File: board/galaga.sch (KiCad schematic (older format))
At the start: 20 parts, among them J1 led_a, J2 speaker_out, J3 led_b, J4 led_c, J5 pwr_in, J6 Conn_02x03_Odd_Even, Q1 IRF540N, SW1 SW_Push, U1 LD1117S33TR_SOT223, U2 ATmega328P-PU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

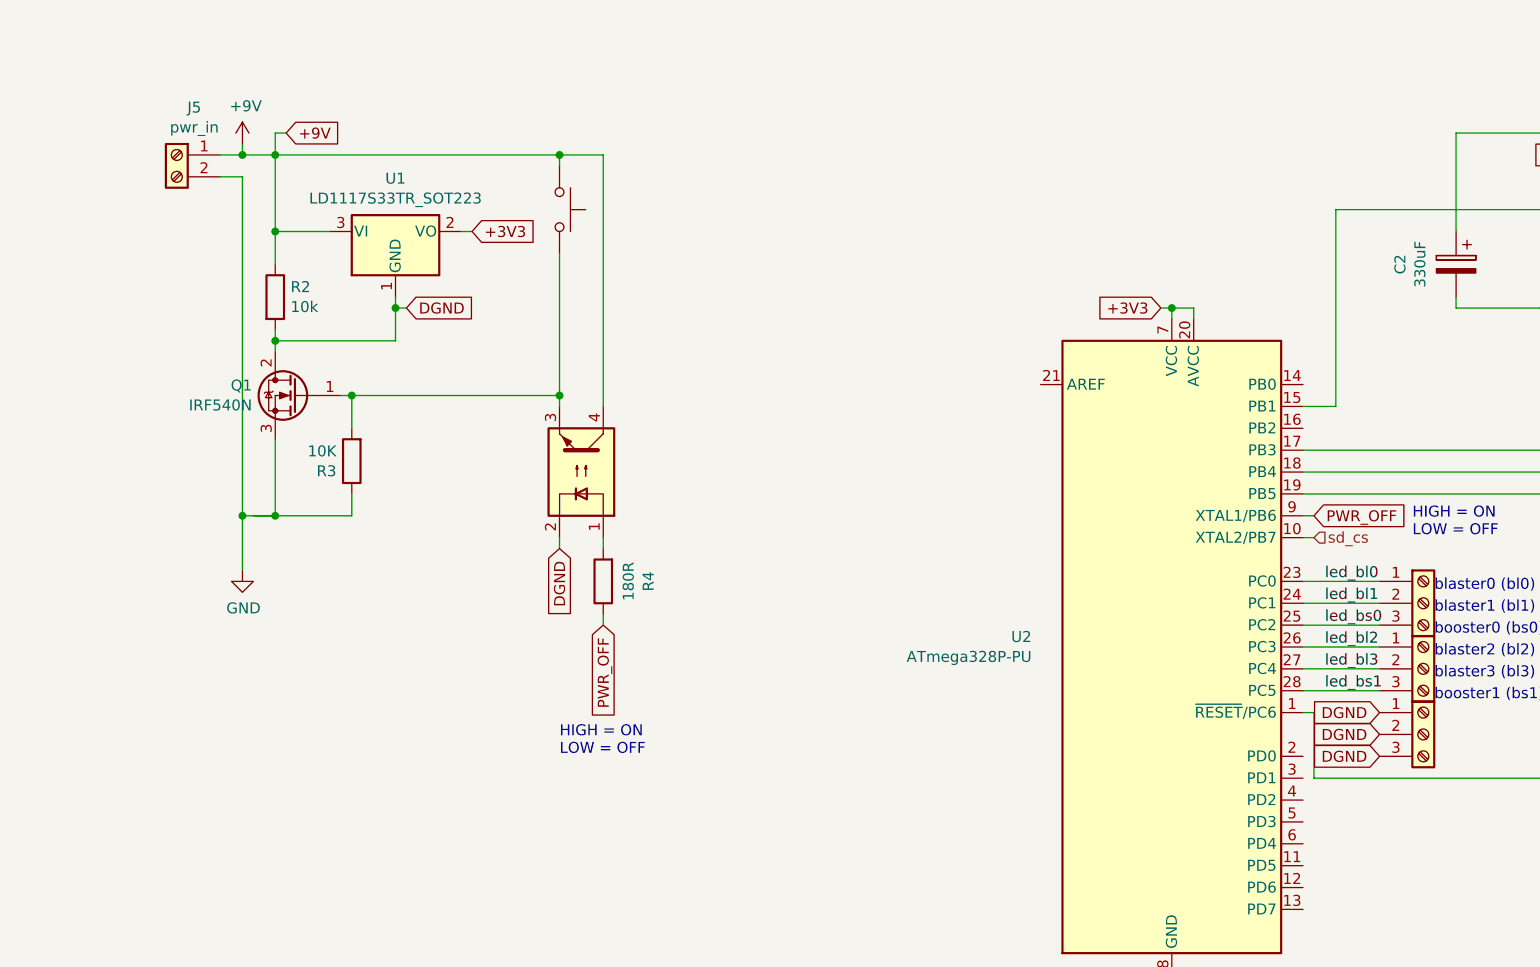
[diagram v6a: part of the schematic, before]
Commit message: RNG tweaked, tested, and working!
All that's really left now is to make the lights flash and assemble
everything. Making the while loop break at the end of file flag instad
of polling seems to have fixed the no-power-off issue - it powered off
perfectly 100 times in a row!
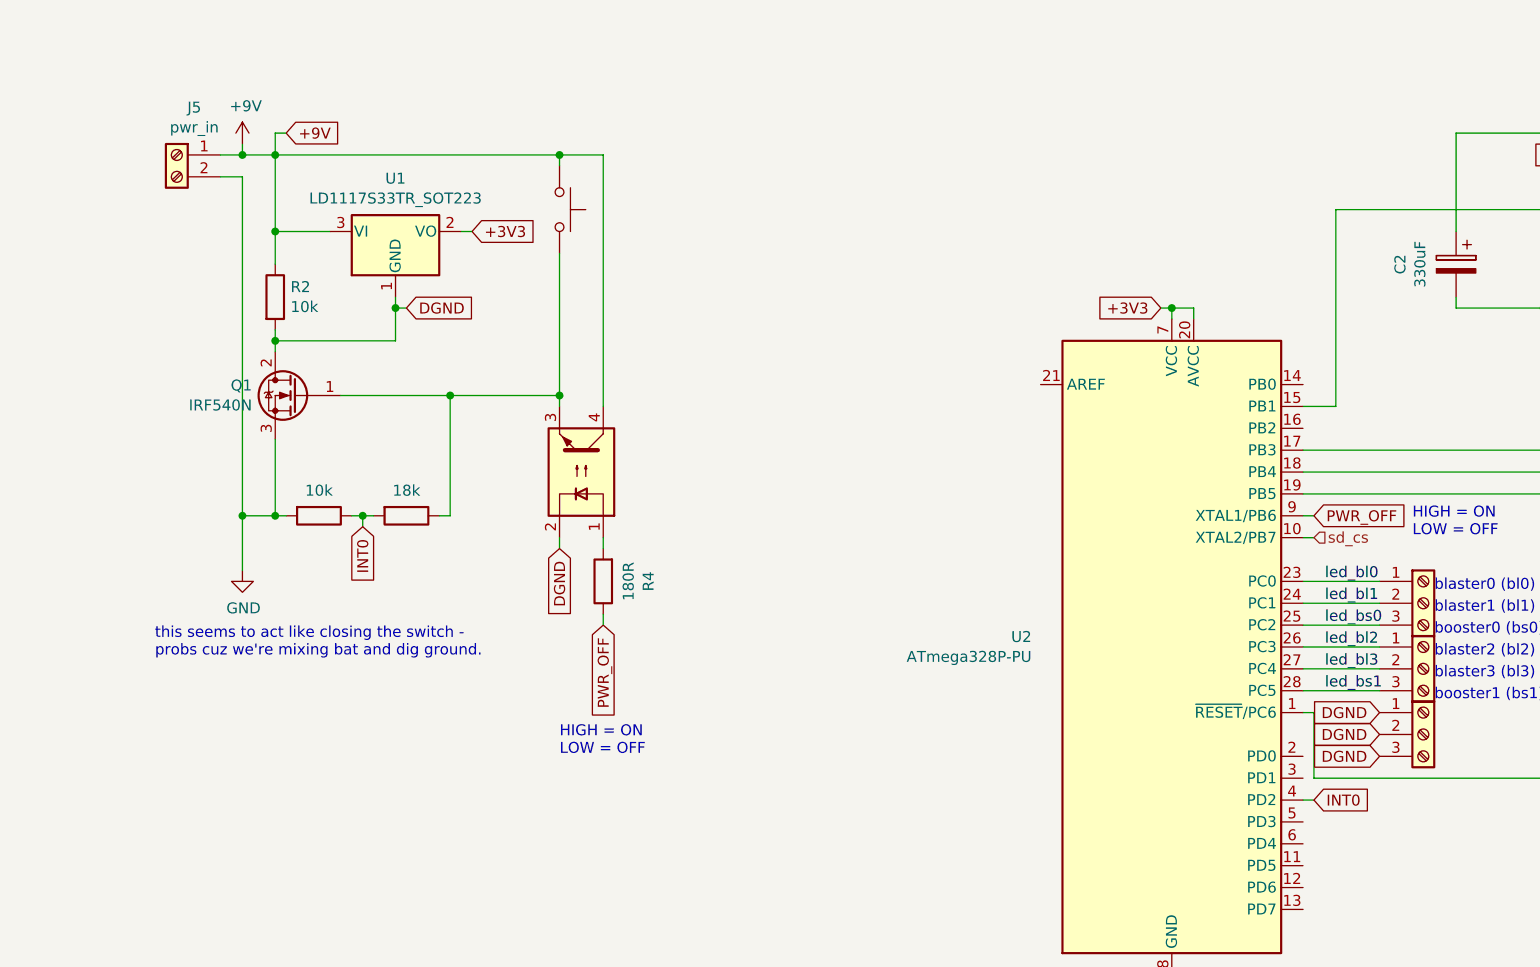
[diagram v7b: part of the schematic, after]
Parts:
- removed R3: 10K, Resistor_THT:R_Axial_DIN0207_L6.3mm_D2.5mm_P2.54mm_Vertical, symbol Device:R
- added R?: 18k, symbol Device:R
- added R?: 10k, symbol Device:R
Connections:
- net GND: now also R?.2
- net INT0: now reaches U2.4 (PD2)
- net INT0: now also R?.1, R?.2
- net at Q1.1 (G), SW1.2, U5.3: now also R?.1
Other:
- note added: "this seems to act like closing the switch -\nprobs cuz we're mixing bat and dig ground."
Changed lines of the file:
@@
-$EndComp
-$Comp
-L Device:R R3
-U 1 1 5D70854B
-P 1700 2250
-F 0 "R3" H 1770 2296 50  0000 L CNN
-F 1 "10K" H 1770 2205 50  0000 L CNN
-F 2 "Resistor_THT:R_Axial_DIN0207_L6.3mm_D2.5mm_P2.54mm_Vertical" V 1630 2250 50  0001 C CNN
-F 3 "~" H 1700 2250 50  0001 C CNN
-	1    1700 2250
-	-1   0    0    1
 $EndComp
 $Comp
@@
 Wire Wire Line
 	1200 850  1350 850
-Connection ~ 1350 2500
 Text GLabel 2650 2650 3    50   Input ~ 0
 DGND
@@
 	2650 2650 2650 2600
 Wire Wire Line
-	1250 2500 1350 2500
-Wire Wire Line
-	1200 2500 1350 2500
-Wire Wire Line
-	1700 2100 1700 1950
-Wire Wire Line
-	1700 1950 1650 1950
-Wire Wire Line
-	1700 2400 1700 2500
-Wire Wire Line
-	1700 2500 1350 2500
-Wire Wire Line
 	1900 1550 1900 1700
 Wire Wire Line
@@
 Wire Wire Line
 	1350 1200 1350 1350
-Connection ~ 1700 1950
 Wire Wire Line
 	1350 850  2650 850
@@
 HIGH = ON\nLOW = OFF
 Connection ~ 2650 850
-Wire Wire Line
-	2650 1300 2650 1950
-Wire Wire Line
-	2650 1950 1700 1950
-Wire Wire Line
-	2650 2000 2650 1950
-Connection ~ 2650 1950
-Wire Wire Line
-	2850 2000 2850 850
-Wire Wire Line
-	2650 850  2850 850
 Text Notes 6550 2600 0    50   ~ 0
 HIGH = ON\nLOW = OFF
@@
 	5550 1550 5550 1600
 Connection ~ 5450 1550
+Text GLabel 6100 3800 2    50   Input ~ 0
+INT0
+Wire Wire Line
+	6050 3800 6100 3800
+Wire Wire Line
+	2650 850  2850 850
+$Comp
+L Device:R R?
+U 1 1 5E33265C
+P 1950 2500
+F 0 "R?" V 1743 2500 50  0001 C CNN
+F 1 "18k" V 1835 2500 50  0000 C CNN
+F 2 "" V 1880 2500 50  0001 C CNN
+F 3 "~" H 1950 2500 50  0001 C CNN
+	1    1950 2500
+	0    1    1    0
+$EndComp
+Text GLabel 1750 2550 3    50   Input ~ 0
+INT0
+$Comp
+L Device:R R?
+U 1 1 5E3398F2
+P 1550 2500
+F 0 "R?" V 1343 2500 50  0001 C CNN
+F 1 "10k" V 1435 2500 50  0000 C CNN
+F 2 "" V 1480 2500 50  0001 C CNN
+F 3 "~" H 1550 2500 50  0001 C CNN
+	1    1550 2500
+	0    1    1    0
+$EndComp
+Connection ~ 2650 1950
+Wire Wire Line
+	2650 1950 2650 2000
+Wire Wire Line
+	1700 2500 1750 2500
+Wire Wire Line
+	1750 2550 1750 2500
+Connection ~ 1750 2500
+Wire Wire Line
+	1750 2500 1800 2500
+Wire Wire Line
+	2650 1300 2650 1950
+Wire Wire Line
+	2850 850  2850 2000
+Wire Wire Line
+	1650 1950 2150 1950
+Wire Wire Line
+	1200 2500 1350 2500
+Wire Wire Line
+	1400 2500 1350 2500
+Connection ~ 1350 2500
+Wire Wire Line
+	2100 2500 2150 2500
+Wire Wire Line
+	2150 2500 2150 1950
+Connection ~ 2150 1950
+Wire Wire Line
+	2150 1950 2650 1950
+Text Notes 800  3150 0    50   ~ 0
+this seems to act like closing the switch -\nprobs cuz we're mixing bat and dig ground.
 $EndSCHEMATC

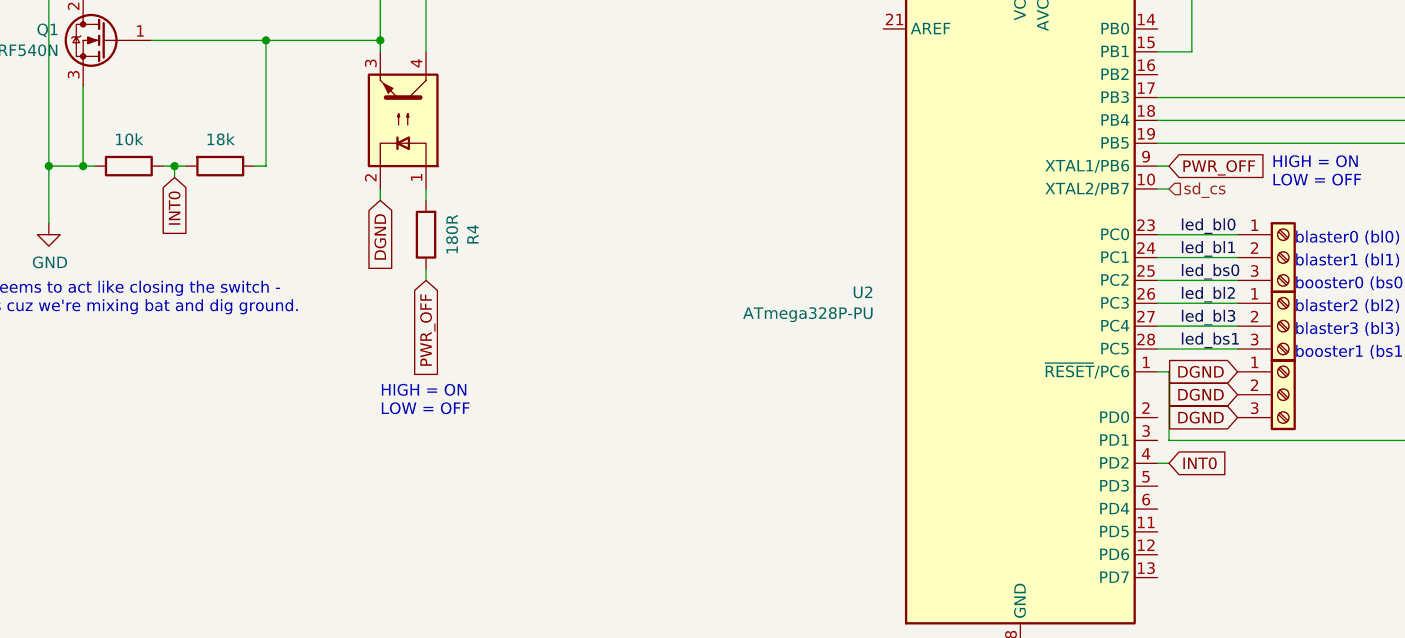
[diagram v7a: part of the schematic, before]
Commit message: led flashing demo implemented, broke rng...
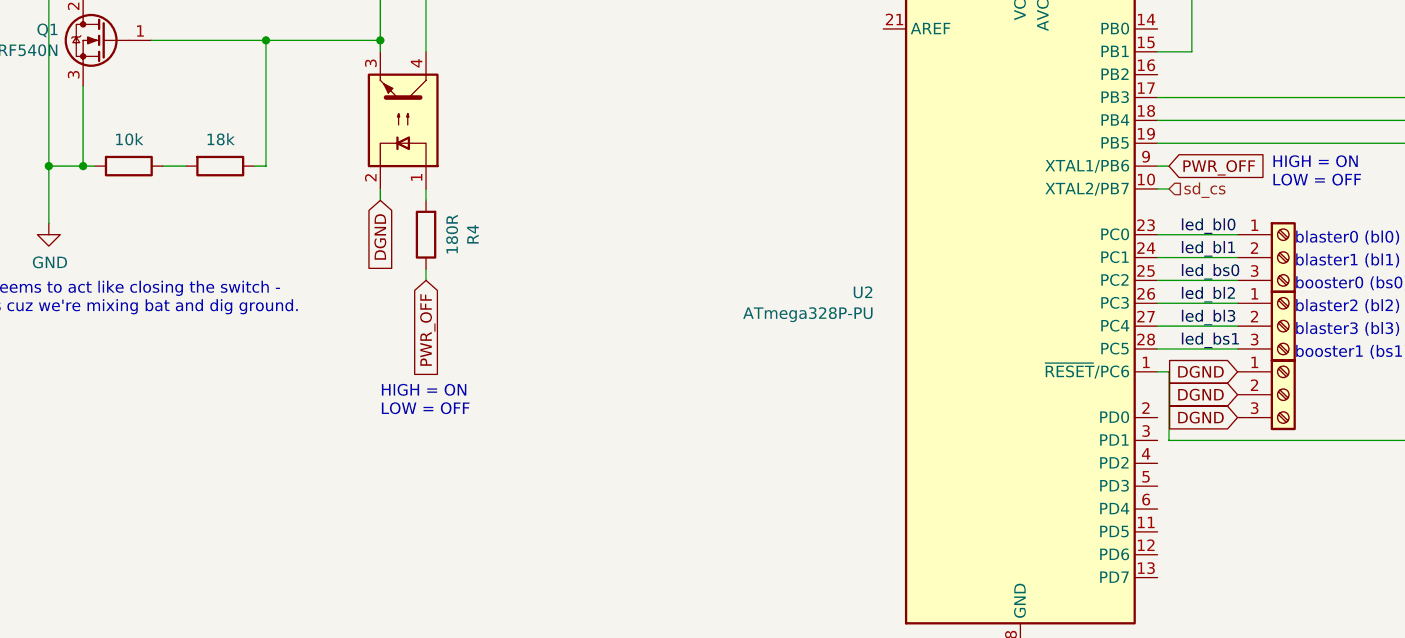
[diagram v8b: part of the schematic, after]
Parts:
- gave numbers to parts that had none: 2
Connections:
- net INT0: no longer names the net of R3.1, R5.2
- net INT0: no longer U2.4 (PD2)
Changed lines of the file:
@@
 	5550 1550 5550 1600
 Connection ~ 5450 1550
-Text GLabel 6100 3800 2    50   Input ~ 0
-INT0
-Wire Wire Line
-	6050 3800 6100 3800
 Wire Wire Line
 	2650 850  2850 850
 $Comp
-L Device:R R?
+L Device:R R5
 U 1 1 5E33265C
 P 1950 2500
-F 0 "R?" V 1743 2500 50  0001 C CNN
+F 0 "R5" V 1743 2500 50  0001 C CNN
 F 1 "18k" V 1835 2500 50  0000 C CNN
 F 2 "" V 1880 2500 50  0001 C CNN
@@
 	0    1    1    0
 $EndComp
-Text GLabel 1750 2550 3    50   Input ~ 0
-INT0
 $Comp
-L Device:R R?
+L Device:R R3
 U 1 1 5E3398F2
 P 1550 2500
-F 0 "R?" V 1343 2500 50  0001 C CNN
+F 0 "R3" V 1343 2500 50  0001 C CNN
 F 1 "10k" V 1435 2500 50  0000 C CNN
 F 2 "" V 1480 2500 50  0001 C CNN
@@
 Wire Wire Line
 	2650 1950 2650 2000
-Wire Wire Line
-	1700 2500 1750 2500
-Wire Wire Line
-	1750 2550 1750 2500
-Connection ~ 1750 2500
-Wire Wire Line
-	1750 2500 1800 2500
 Wire Wire Line
 	2650 1300 2650 1950
@@
 Text Notes 800  3150 0    50   ~ 0
 this seems to act like closing the switch -\nprobs cuz we're mixing bat and dig ground.
+Wire Wire Line
+	1700 2500 1800 2500
 $EndSCHEMATC
